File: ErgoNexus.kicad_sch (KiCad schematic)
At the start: 130 parts, among them J10 Conn_01x06, J7 Conn_01x02, J8 Conn_01x02, J9 Conn_01x06, SW1 SW_Push, SW2 RotaryEncoder_Switch, SW3 SW_Push, SW4 RotaryEncoder_Switch, U1 SuperMini nRF52840, U2 SuperMini nRF52840

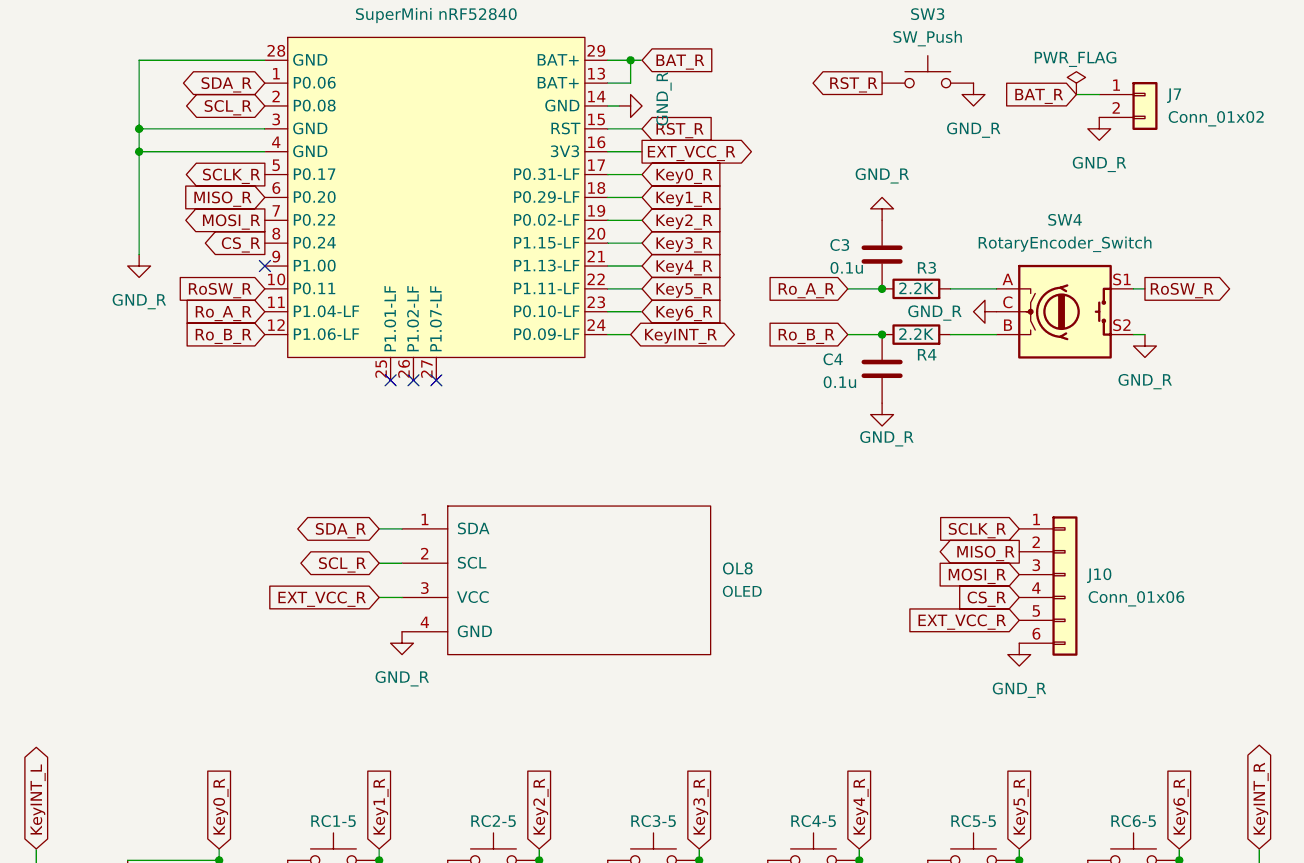
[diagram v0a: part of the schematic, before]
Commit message: fix: 右手の配線を完成
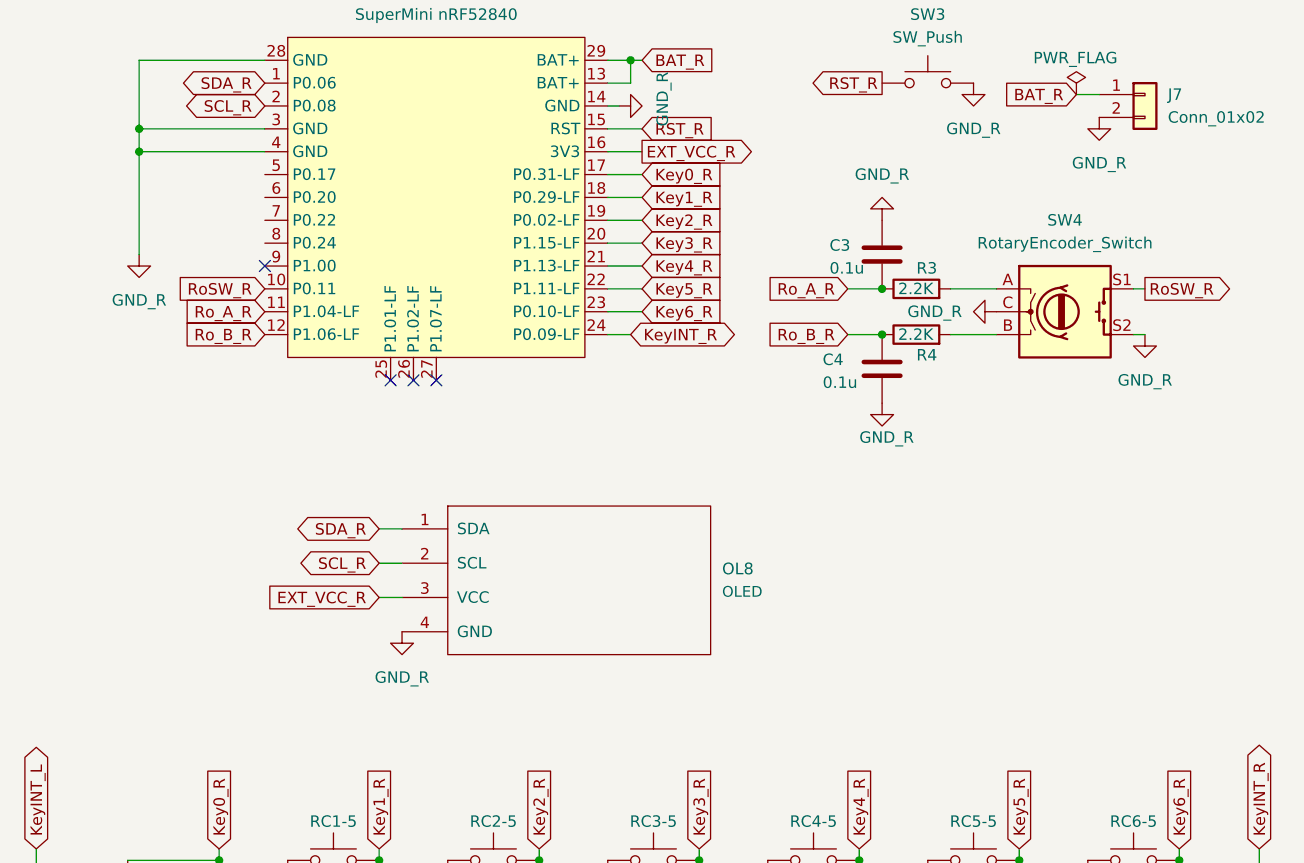
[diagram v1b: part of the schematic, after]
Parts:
- removed J10: Conn_01x06, Connector_PinHeader_2.54mm:PinHeader_1x06_P2.54mm_Horizontal, symbol Connector_Generic:Conn_01x06
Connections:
- net CS_R: no longer names the net of U2.8 (P0.24)
- net MISO_R: no longer names the net of U2.6 (P0.20)
- net MOSI_R: no longer names the net of U2.7 (P0.22)
- net SCLK_R: no longer names the net of U2.5 (P0.17)

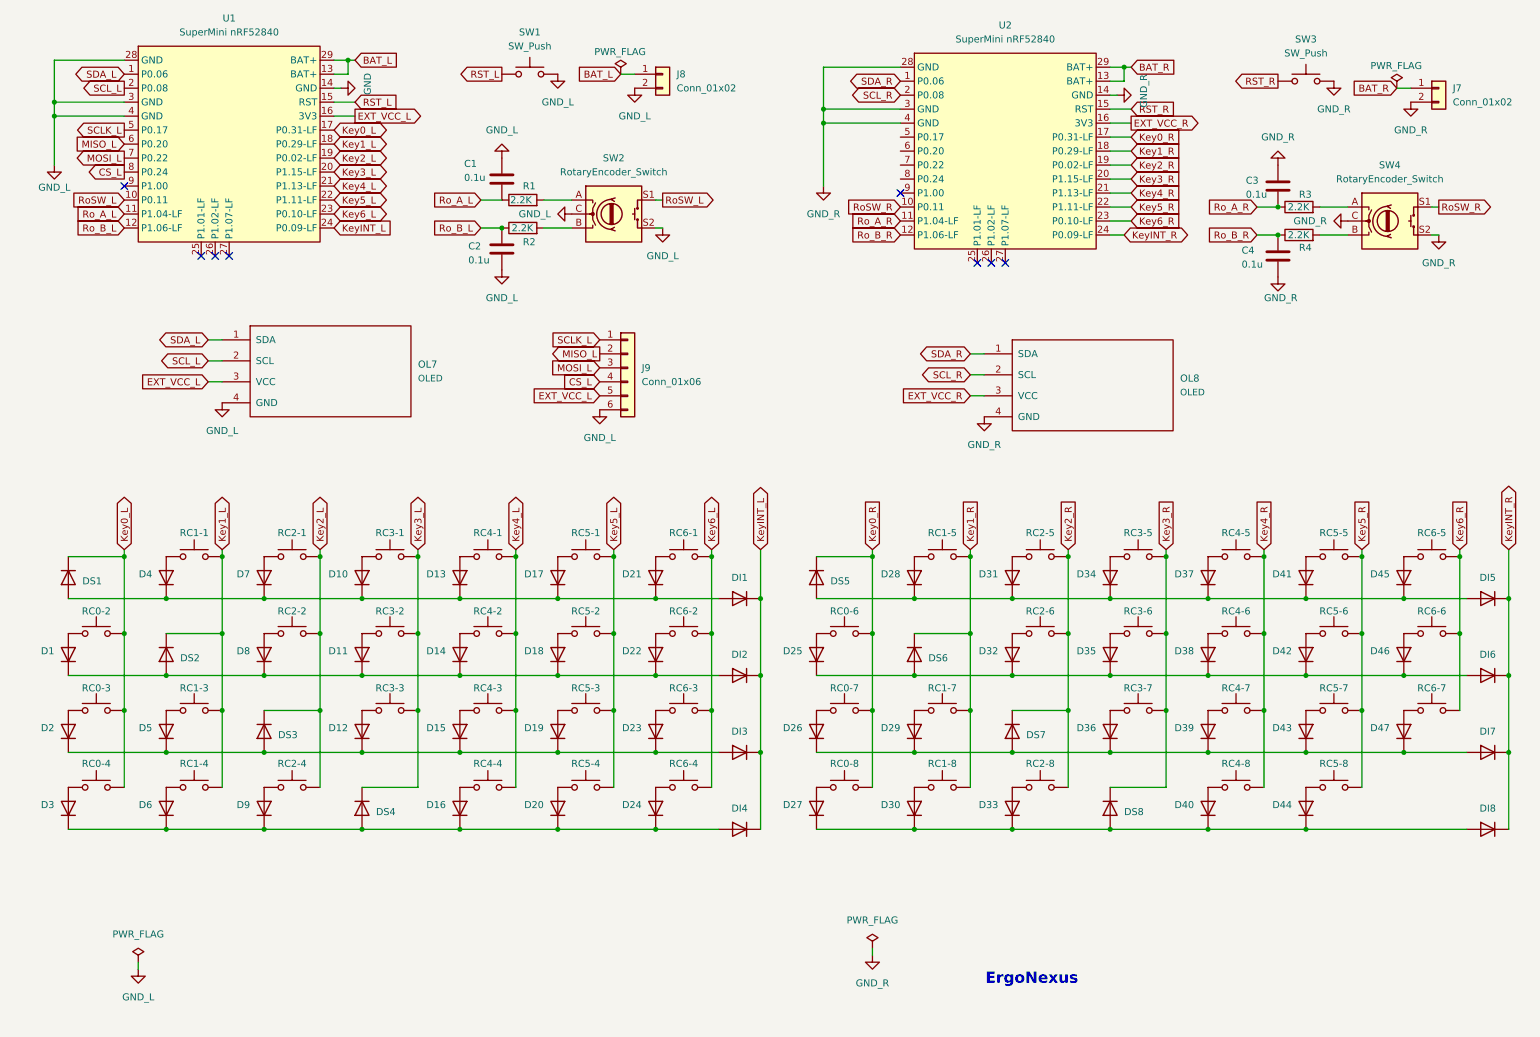
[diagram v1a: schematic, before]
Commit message: feat: 回路図においてキースイッチをマトリックス配列に変更
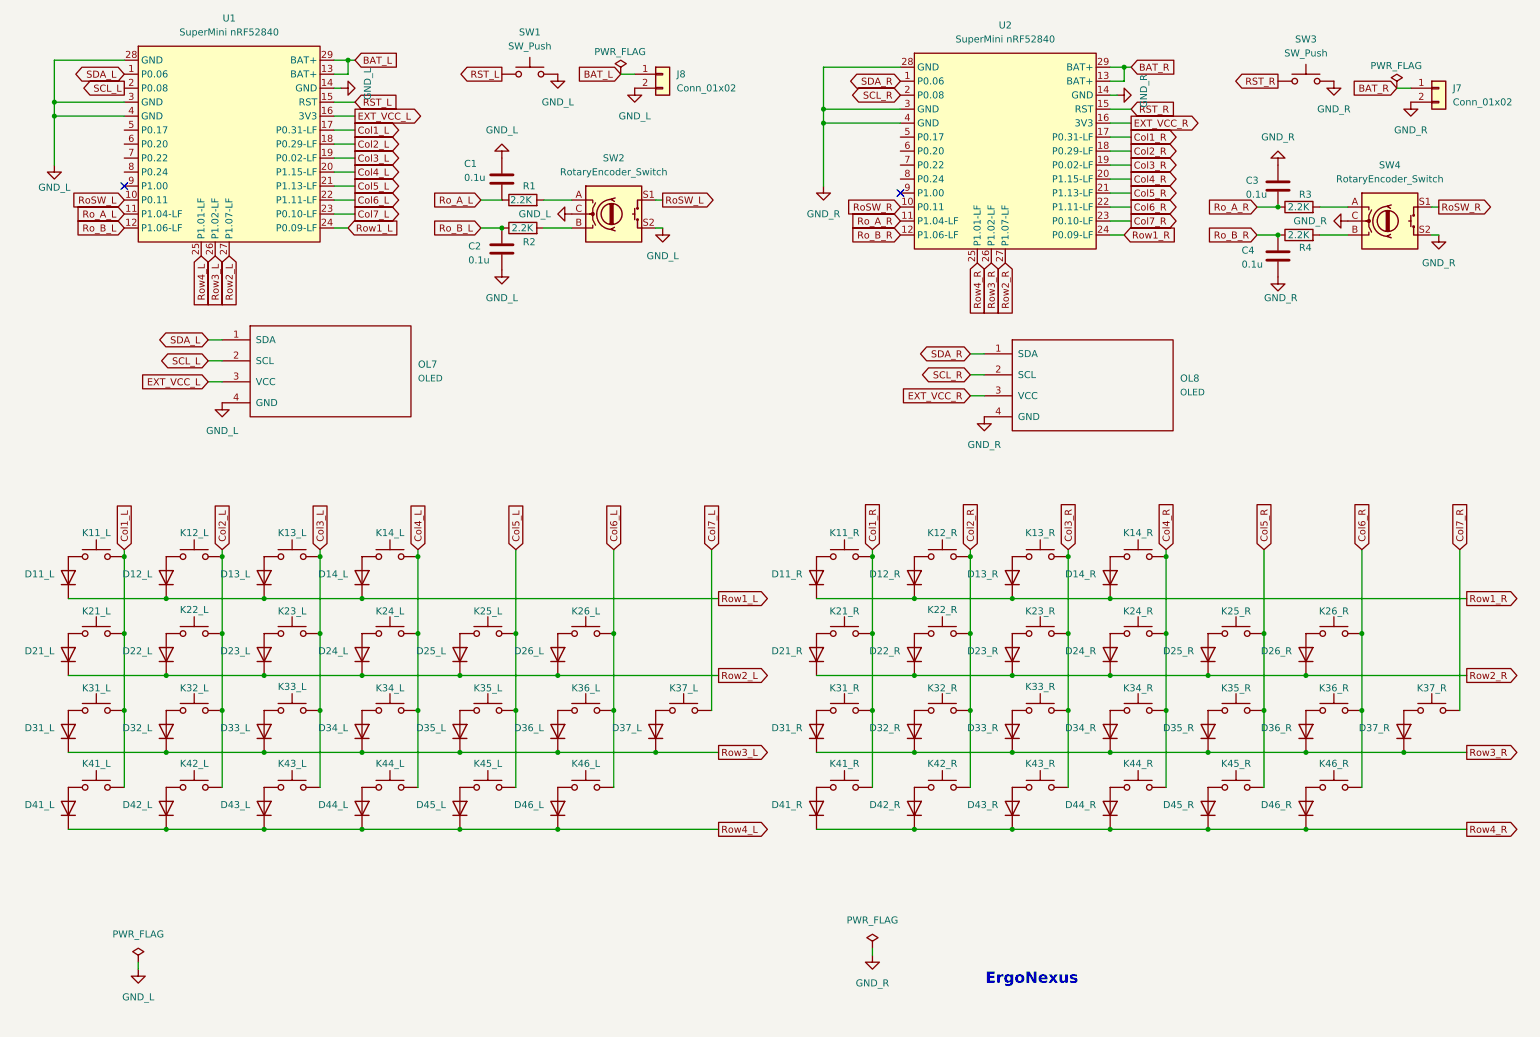
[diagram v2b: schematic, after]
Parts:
- removed D1, D10, D11, D12, D13, D14, D15, D16, D17, D18, D19, D2, D20, D21, D22, D23, D24, D3, D37, D4, D41, D45, D46, D5, D6, D7, D8, D9, DI1, DI2, DI3, DI4, DI5, DI6, DI7, DI8, DS1, DS2, DS3, DS4, DS5, DS6, DS7, DS8: 1N4148, kbd_Parts:Diode_TH_SMD, symbol Diode:1N4148
- removed J9: Conn_01x06, Connector_PinHeader_2.54mm:PinHeader_1x06_P2.54mm_Horizontal, symbol Connector_Generic:Conn_01x06
- removed RC0-2, RC0-3, RC0-4, RC1-1, RC1-3, RC1-4, RC2-1, RC2-2, RC2-4, RC3-1, RC3-2, RC3-3, RC4-1, RC4-2, RC4-3, RC4-4, RC4-5, RC5-1, RC5-2, RC5-3, RC5-4, RC5-5, RC6-1, RC6-2, RC6-3, RC6-4, RC6-5, RC6-6: SW_Push, kbd_SW:CherryMX_Hotswap_1u, symbol Switch:SW_Push
- added D11_L, D11_R, D12_L, D13_L, D14_L, D21_L, D22_L, D22_R, D23_L, D24_L, D25_L, D26_L, D31_L, D32_L, D33_L, D33_R, D34_L, D35_L, D36_L, D37_L, D41_L, D42_L, D43_L, D44_L, D44_R, D45_L, D46_L: 1N4148, kbd_Parts:Diode_TH_SMD, symbol Diode:1N4148
- added K11_L, K11_R, K12_L, K13_L, K14_L, K21_L, K22_L, K22_R, K23_L, K24_L, K25_L, K26_L, K31_L, K32_L, K33_L, K33_R, K34_L, K35_L, K36_L, K37_L, K41_L, K42_L, K43_L, K44_L, K44_R, K45_L, K46_L: SW_Push, kbd_SW:CherryMX_Hotswap_1u, symbol Switch:SW_Push
- renumbered D28 to D12_R, D31 to D13_R, D34 to D14_R, D25 to D21_R, D32 to D23_R, D35 to D24_R, D38 to D25_R, D42 to D26_R, D26 to D31_R, D29 to D32_R, D36 to D34_R, D39 to D35_R, D43 to D36_R, D47 to D37_R, D27 to D41_R, D30 to D42_R, D33 to D43_R, D40 to D45_R, D44 to D46_R, RC1-5 to K12_R, RC2-5 to K13_R, RC3-5 to K14_R, RC0-6 to K21_R, RC2-6 to K23_R, RC3-6 to K24_R, RC4-6 to K25_R, RC5-6 to K26_R, RC0-7 to K31_R, RC1-7 to K32_R, RC3-7 to K34_R, RC4-7 to K35_R, RC5-7 to K36_R, RC6-7 to K37_R, RC0-8 to K41_R, RC1-8 to K42_R, RC2-8 to K43_R, RC4-8 to K45_R, RC5-8 to K46_R
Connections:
- net GND is gone; now on net GND_L: U1.14 (GND)
- net KeyINT_R is gone; now on net Row1_R: U2.24 (P0.09-LF)
- net Row2_R: now reaches D21_R.1 (K), D23_R.1 (K), D24_R.1 (K), D25_R.1 (K), D26_R.1 (K)
- net Row2_R: now also U2.27 (P1.07-LF), D22_R.1 (K)
- net Row1_R: now reaches D12_R.1 (K), D13_R.1 (K), D14_R.1 (K)
- net Row1_R: now also D11_R.1 (K)
- net Row3_R: now reaches D31_R.1 (K), D32_R.1 (K), D34_R.1 (K), D35_R.1 (K), D36_R.1 (K), D37_R.1 (K)
- net Row3_R: now also U2.26 (P1.02-LF), D33_R.1 (K)
- net Row4_R: now reaches U2.25 (P1.01-LF)
- net Row4_R: now also D41_R.1 (K), D42_R.1 (K), D43_R.1 (K), D45_R.1 (K), D46_R.1 (K), D44_R.1 (K)
- net Row4_L: now reaches U1.25 (P1.01-LF)
- net Row4_L: now also D41_L.1 (K), D42_L.1 (K), D43_L.1 (K), D44_L.1 (K), D45_L.1 (K), D46_L.1 (K)
- net Row3_L: now reaches U1.26 (P1.02-LF)
- net Row3_L: now also D31_L.1 (K), D32_L.1 (K), D33_L.1 (K), D34_L.1 (K), D35_L.1 (K), D36_L.1 (K), D37_L.1 (K)
- net Row2_L: now reaches U1.27 (P1.07-LF)
- net Row2_L: now also D21_L.1 (K), D22_L.1 (K), D23_L.1 (K), D24_L.1 (K), D25_L.1 (K), D26_L.1 (K)
- net CS_L: no longer names the net of U1.8 (P0.24)
- net Key0_L renamed Col1_L
- net Col1_L: now also K11_L.1, K21_L.1, K31_L.1, K41_L.1
- net Key0_R renamed Col1_R
- net Col1_R: now also K11_R.1
- net Key1_L renamed Col2_L
- net Col2_L: now also K12_L.1, K22_L.1, K32_L.1, K42_L.1
- net Key1_R renamed Col2_R
- net Col2_R: now also K22_R.1
- net Key2_L renamed Col3_L
- net Col3_L: now also K13_L.1, K23_L.1, K33_L.1, K43_L.1
- net Key2_R renamed Col3_R
- net Col3_R: now also K33_R.1
- net Key3_L renamed Col4_L
- net Col4_L: now also K14_L.1, K24_L.1, K34_L.1, K44_L.1
- net Key3_R renamed Col4_R
- net Col4_R: now also K44_R.1
- net Key4_L renamed Col5_L
- net Col5_L: now also K25_L.1, K35_L.1, K45_L.1
- net Key4_R renamed Col5_R
- net Key5_L renamed Col6_L
- net Col6_L: now also K26_L.1, K36_L.1, K46_L.1
- net Key5_R renamed Col6_R
- net Key6_L renamed Col7_L
- net Col7_L: now also K37_L.1
- net Key6_R renamed Col7_R
- net KeyINT_L renamed Row1_L
- net Row1_L: now also D11_L.1 (K), D12_L.1 (K), D13_L.1 (K), D14_L.1 (K)
- net MISO_L: no longer names the net of U1.6 (P0.20)
- net MOSI_L: no longer names the net of U1.7 (P0.22)
- net SCLK_L: no longer names the net of U1.5 (P0.17)
- new net: D31_L.2 (A), K31_L.2
- new net: D45_L.2 (A), K45_L.2
- new net: D14_L.2 (A), K14_L.2
- new net: D11_R.2 (A), K11_R.2
- new net: D22_R.2 (A), K22_R.2
- new net: D21_L.2 (A), K21_L.2
- new net: D33_L.2 (A), K33_L.2
- new net: D46_L.2 (A), K46_L.2
- new net: D22_L.2 (A), K22_L.2
- new net: D43_L.2 (A), K43_L.2
- new net: D42_L.2 (A), K42_L.2
- new net: D23_L.2 (A), K23_L.2
- new net: D33_R.2 (A), K33_R.2
- new net: D36_L.2 (A), K36_L.2
- new net: D13_L.2 (A), K13_L.2
- new net: D32_L.2 (A), K32_L.2
- new net: D12_L.2 (A), K12_L.2
- new net: D37_L.2 (A), K37_L.2
- new net: D44_R.2 (A), K44_R.2
- new net: D44_L.2 (A), K44_L.2
- new net: D25_L.2 (A), K25_L.2
- new net: D26_L.2 (A), K26_L.2
- new net: D35_L.2 (A), K35_L.2
- new net: D24_L.2 (A), K24_L.2
- new net: D34_L.2 (A), K34_L.2
- new net: D41_L.2 (A), K41_L.2
- new net: D11_L.2 (A), K11_L.2
- no-connect marks 8 -> 2

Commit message: fix: not fully annotation
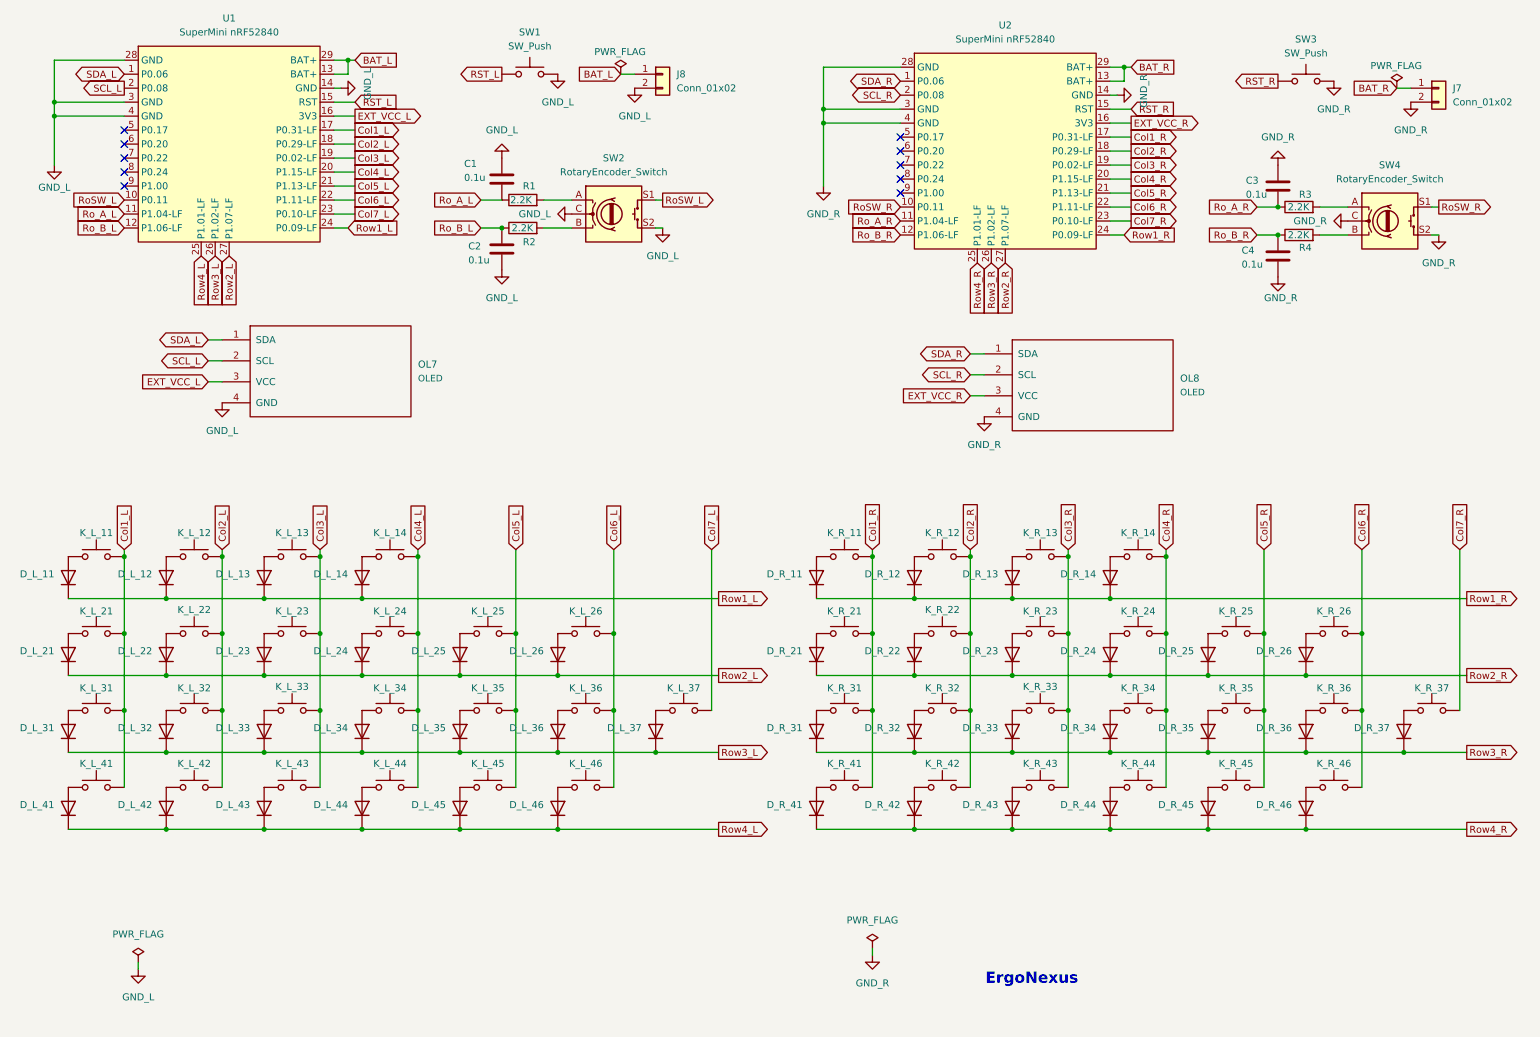
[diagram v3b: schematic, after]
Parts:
- removed D11_L: 1N4148, kbd_Parts:Diode_TH_SMD, symbol Diode:1N4148
- added D_L_11: 1N4148, kbd_Parts:Diode_TH_SMD, symbol Diode:1N4148
- renumbered D12_L to D_L_12, D13_L to D_L_13, D14_L to D_L_14, D21_L to D_L_21, D22_L to D_L_22, D23_L to D_L_23, D24_L to D_L_24, D25_L to D_L_25, D26_L to D_L_26, D31_L to D_L_31, D32_L to D_L_32, D33_L to D_L_33, D34_L to D_L_34, D35_L to D_L_35, D36_L to D_L_36, D37_L to D_L_37, D41_L to D_L_41, D42_L to D_L_42, D43_L to D_L_43, D44_L to D_L_44, D45_L to D_L_45, D46_L to D_L_46, D11_R to D_R_11, D12_R to D_R_12, D13_R to D_R_13, D14_R to D_R_14, D21_R to D_R_21, D22_R to D_R_22, D23_R to D_R_23, D24_R to D_R_24, D25_R to D_R_25, D26_R to D_R_26, D31_R to D_R_31, D32_R to D_R_32, D33_R to D_R_33, D34_R to D_R_34, D35_R to D_R_35, D36_R to D_R_36, D37_R to D_R_37, D41_R to D_R_41, D42_R to D_R_42, D43_R to D_R_43, D44_R to D_R_44, D45_R to D_R_45, D46_R to D_R_46, K11_L to K_L_11, K12_L to K_L_12, K13_L to K_L_13, K14_L to K_L_14, K21_L to K_L_21, K22_L to K_L_22, K23_L to K_L_23, K24_L to K_L_24, K25_L to K_L_25, K26_L to K_L_26, K31_L to K_L_31, K32_L to K_L_32, K33_L to K_L_33, K34_L to K_L_34, K35_L to K_L_35, K36_L to K_L_36, K37_L to K_L_37, K41_L to K_L_41, K42_L to K_L_42, K43_L to K_L_43, K44_L to K_L_44, K45_L to K_L_45, K46_L to K_L_46, K11_R to K_R_11, K12_R to K_R_12, K13_R to K_R_13, K14_R to K_R_14, K21_R to K_R_21, K22_R to K_R_22, K23_R to K_R_23, K24_R to K_R_24, K25_R to K_R_25, K26_R to K_R_26, K31_R to K_R_31, K32_R to K_R_32, K33_R to K_R_33, K34_R to K_R_34, K35_R to K_R_35, K36_R to K_R_36, K37_R to K_R_37, K41_R to K_R_41, K42_R to K_R_42, K43_R to K_R_43, K44_R to K_R_44, K45_R to K_R_45, K46_R to K_R_46
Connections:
- net Row1_L: now also D_L_11.1 (K)
- net at K_L_11.2: now also D_L_11.2 (A)
- no-connect marks 2 -> 10
